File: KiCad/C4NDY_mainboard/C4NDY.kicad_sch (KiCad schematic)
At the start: 45 parts, among them J1 Conn_01x08, J2 Conn_01x07, J3 Conn_01x05, J4 5077CR-16SMC2-BK-TR, J5 Conn_01x06, J6 Conn_01x08, J7 FTSH-105-01-L-DV-K, SW1 SKRPABE010, SW2 SKRPABE010, U1 MIC39100-3.3WS, U2 IS66WVS2M8BLL, U3 STM32G4A1CETx, X1 SG-310SCF

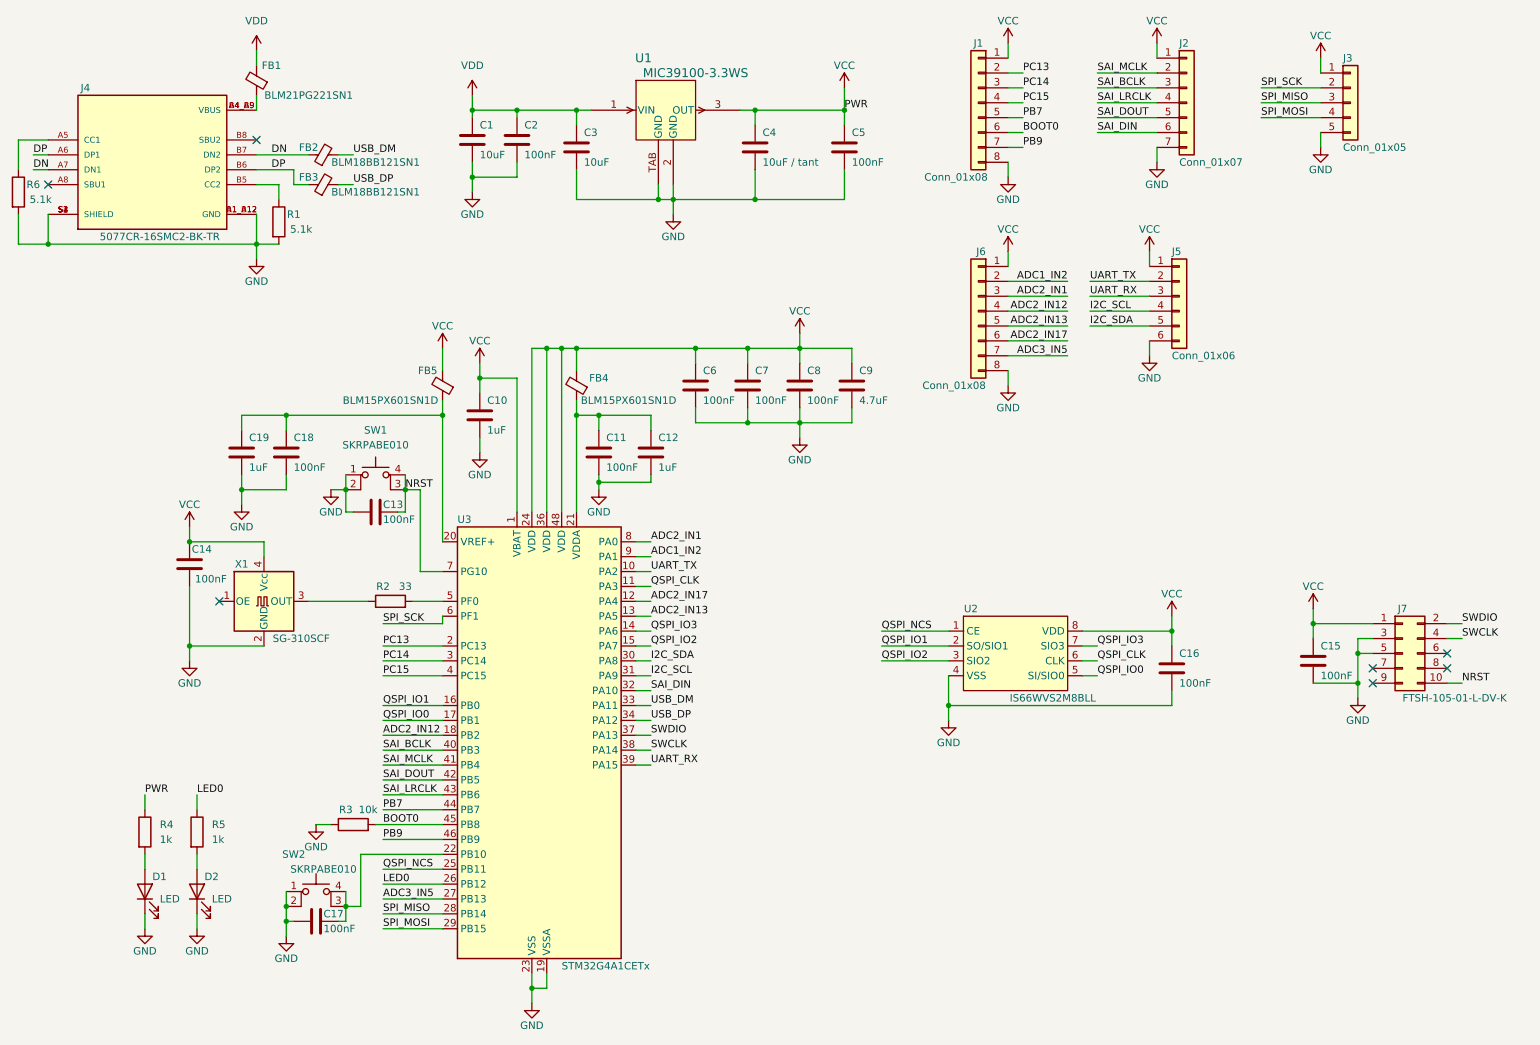
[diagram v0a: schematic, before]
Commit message: SWD用のコネクタを汎用のピンヘッダに変更し、viaをテントに修正。
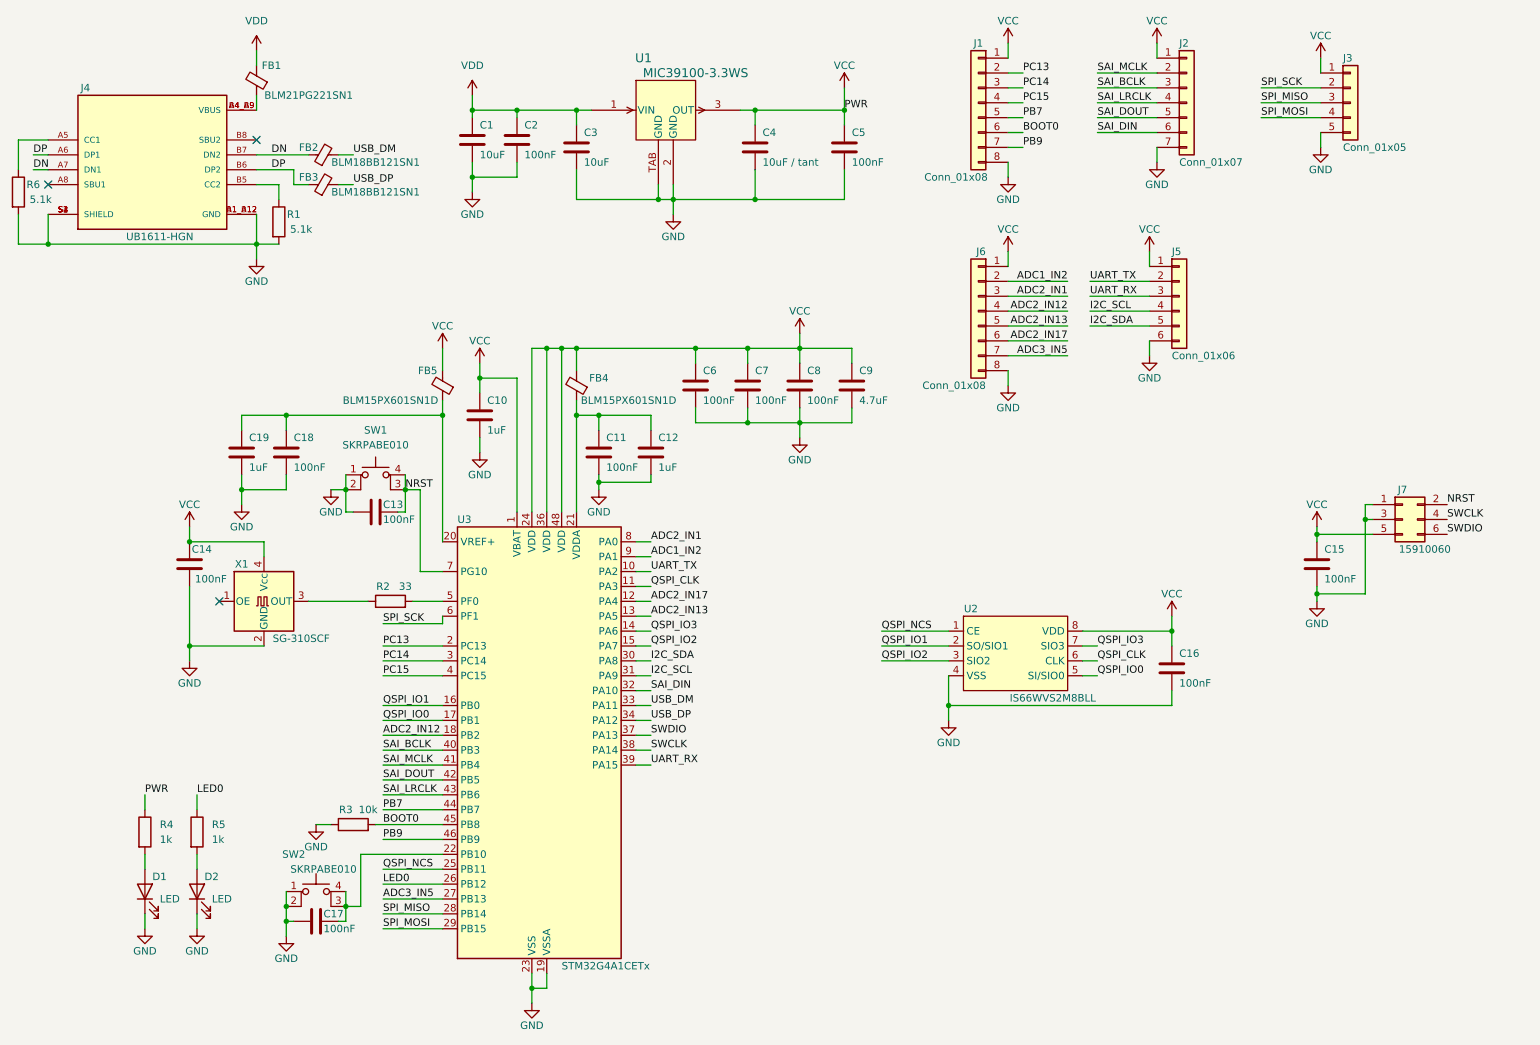
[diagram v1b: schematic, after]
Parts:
- removed J7: FTSH-105-01-L-DV-K, My_Parts:SAMTEC_FTSH-105-XX-X-DV, symbol Connector_Generic:Conn_02x05_Odd_Even
- added J7: 15910060, My_Parts:Molex_15910060, symbol Connector_Generic:Conn_02x03_Odd_Even
- J4: value 5077CR-16SMC2-BK-TR -> UB1611-HGN; footprint My_Parts:NELTRON_5077CR-16SMC2-BK-TR -> My_Parts:Gangyuan_UB1611-HGN; MANUFACTURER Neltron -> Gangyuan; SNAPEDA_PN 5077CR-16SMC2-BK-TR -> UB1611-HGN
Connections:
- net GND: now also J7.1 (Pin_1), J7.3 (Pin_3)
- net NRST: now also J7.2 (Pin_2)
- net SWCLK: now also J7.4 (Pin_4)
- net SWDIO: now also J7.6 (Pin_6)
- net VCC: now also J7.5 (Pin_5)
- no-connect marks 7 -> 3
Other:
- moved on the sheet: C15

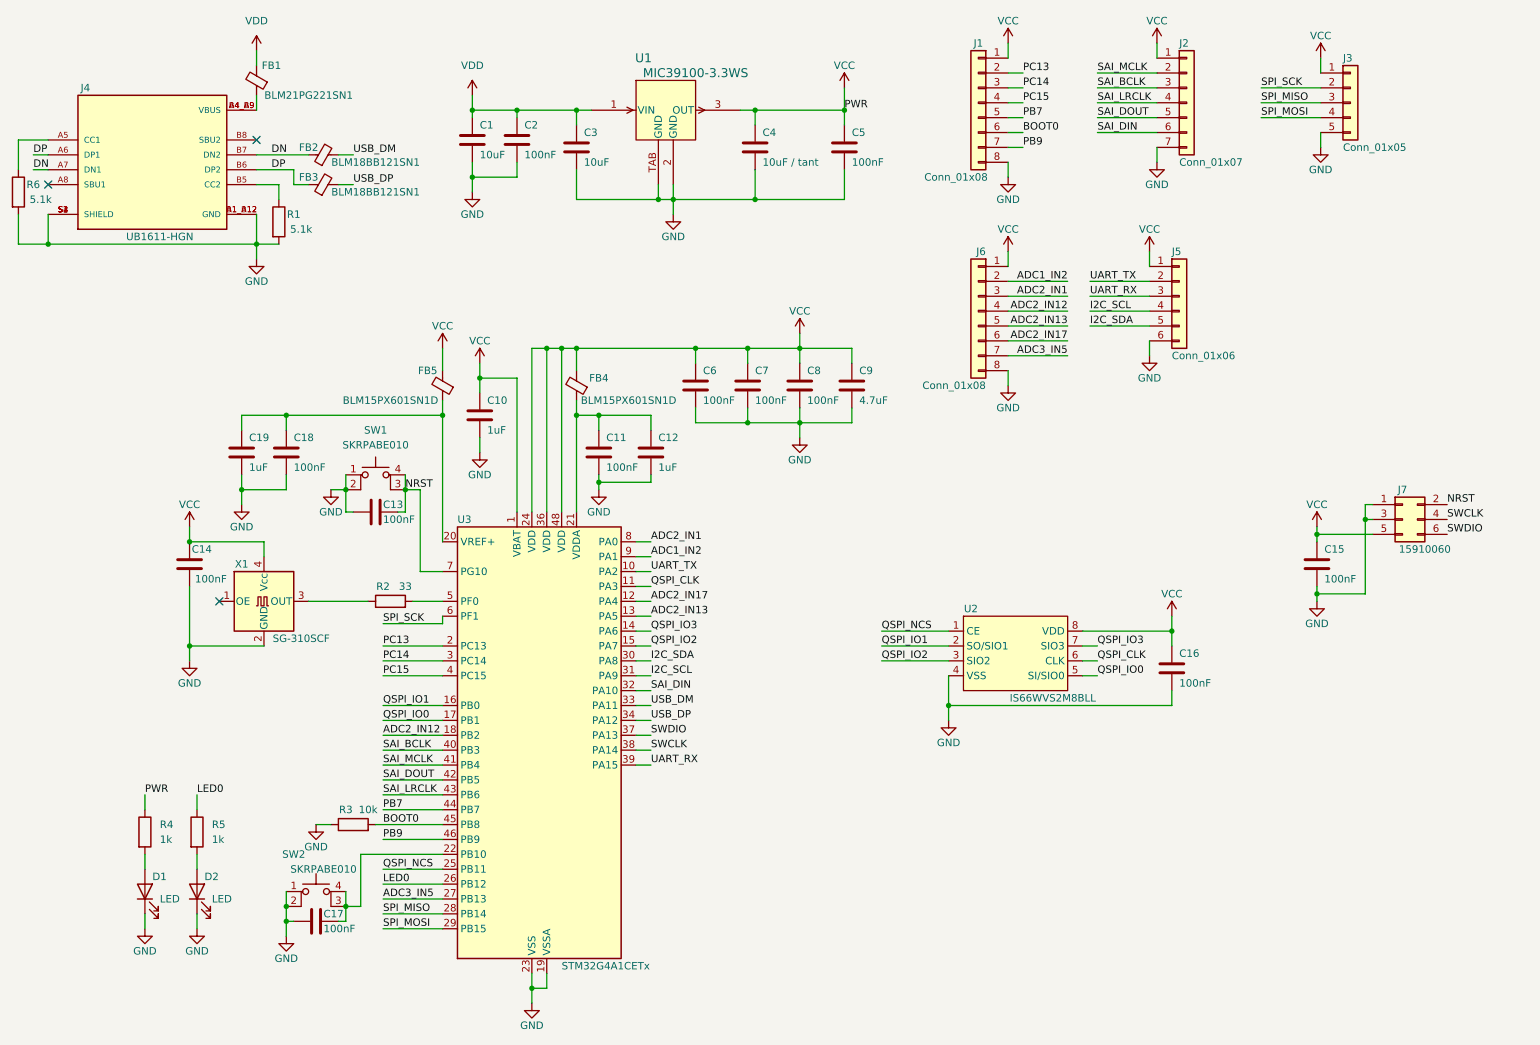
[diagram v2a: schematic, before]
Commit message: Added TPS2116 and removed onboard QSPI..
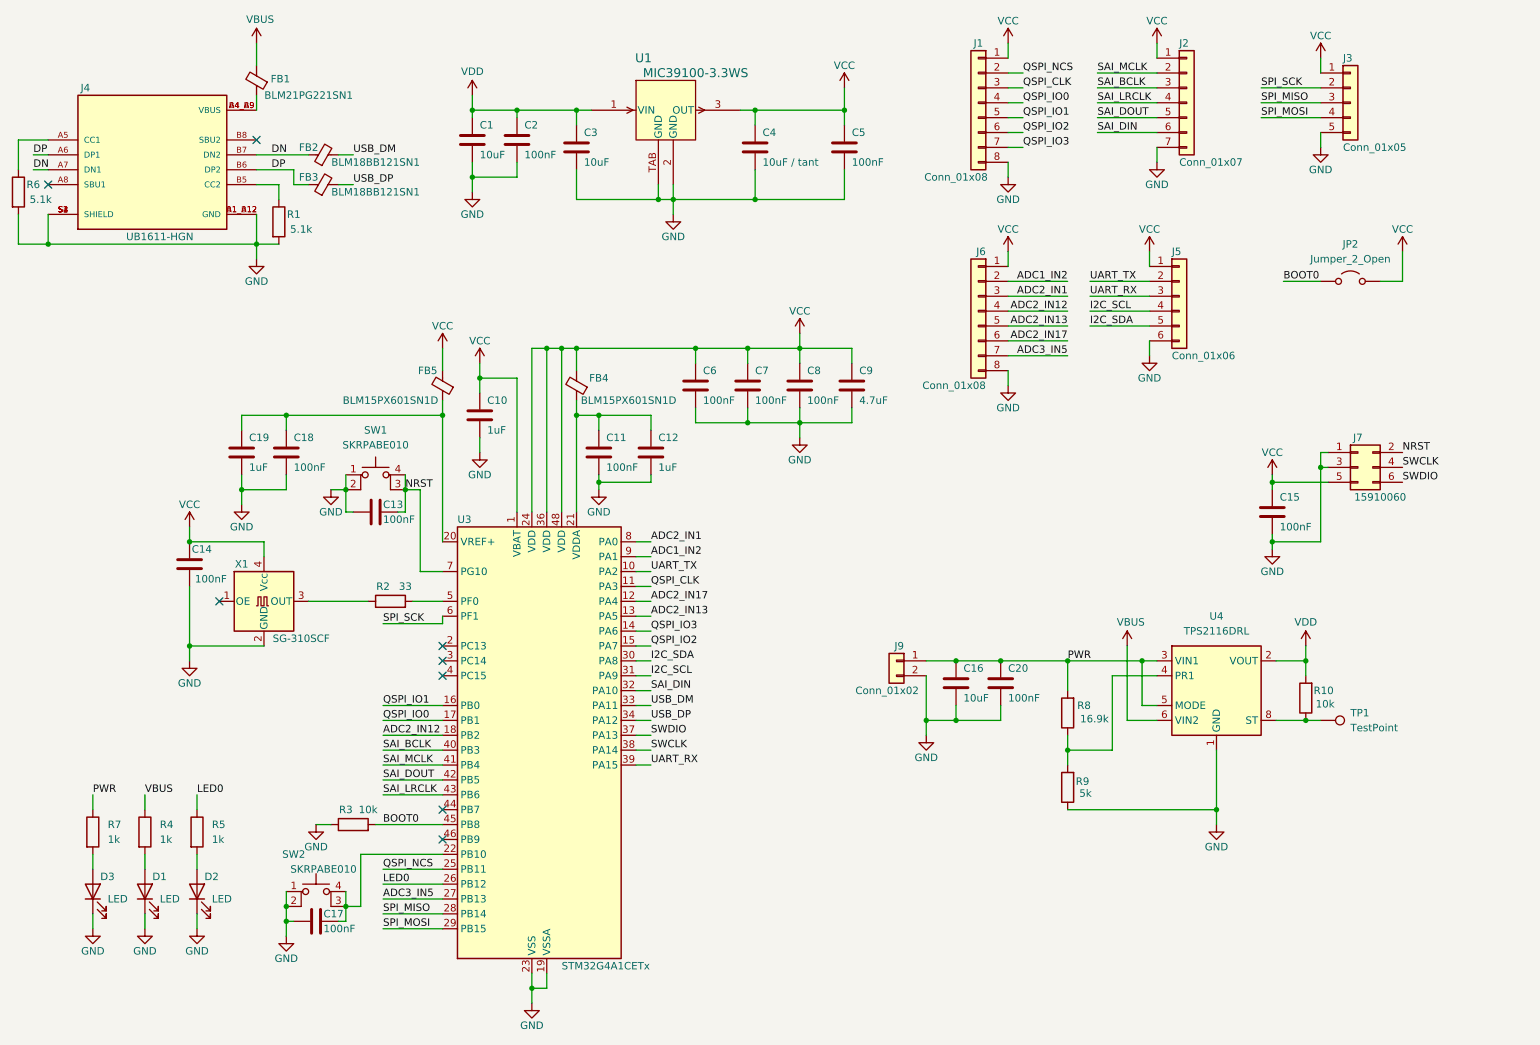
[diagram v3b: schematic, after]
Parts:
- removed U2: IS66WVS2M8BLL, Package_SO:SOIC-8_3.9x4.9mm_P1.27mm, symbol My_Parts:SRAM_QSPI
- added C20: 100nF, Capacitor_SMD:C_0603_1608Metric, symbol Device:C
- added D3: LED, LED_SMD:LED_0603_1608Metric, symbol Device:LED
- added J9: Conn_01x02, My_Parts:PinHeader_1x02_P2.54mm_Vertical, symbol Connector_Generic:Conn_01x02
- added JP2: Jumper_2_Open, Jumper:SolderJumper-2_P1.3mm_Open_RoundedPad1.0x1.5mm, symbol Jumper:Jumper_2_Open
- added R10: 10k, Resistor_SMD:R_0402_1005Metric, symbol Device:R
- added R7: 1k, Resistor_SMD:R_0402_1005Metric, symbol Device:R
- added R8: 16.9k, Resistor_SMD:R_0402_1005Metric, symbol Device:R
- added R9: 5k, Resistor_SMD:R_0402_1005Metric, symbol Device:R
- added TP1: TestPoint, TestPoint:TestPoint_THTPad_1.0x1.0mm_Drill0.5mm, symbol Connector:TestPoint
- added U4: TPS2116DRL, My_Parts:SOT-583-8, symbol Power_Management:TPS2116DRL
- C16: value 100nF -> 10uF; footprint Capacitor_SMD:C_0402_1005Metric -> Capacitor_SMD:C_0603_1608Metric
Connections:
- net BOOT0: now also JP2.1 (A); no longer J1.6 (Pin_6)
- net GND: now also C20.2, D3.1 (K), J9.2 (Pin_2), R9.1, U4.1 (GND)
- net QSPI_CLK: now also J1.3 (Pin_3)
- net QSPI_IO0: now also J1.4 (Pin_4)
- net QSPI_IO1: now also J1.5 (Pin_5)
- net QSPI_IO2: now also J1.6 (Pin_6)
- net QSPI_IO3: now also J1.7 (Pin_7)
- net QSPI_NCS: now also J1.2 (Pin_2)
- net VCC: now also JP2.2 (B); no longer C16.1, R4.1
- net VDD: now also R10.2, U4.2 (VOUT), U4.7 (VOUT); no longer FB1.2
- net PB7: no longer names the net of U3.44 (PB7)
- net PB7: no longer J1.5 (Pin_5)
- net PB9: no longer names the net of U3.46 (PB9)
- net PB9: no longer J1.7 (Pin_7)
- net PC13: no longer names the net of U3.2 (PC13)
- net PC13: no longer J1.2 (Pin_2)
- net PC14: no longer names the net of U3.3 (PC14)
- net PC14: no longer J1.3 (Pin_3)
- net PC15: no longer names the net of U3.4 (PC15)
- net PC15: no longer J1.4 (Pin_4)
- new net: R10.1, TP1.1, U4.8 (ST)
- new net: D3.2 (A), R7.2
- new net: R8.1, R9.2, U4.4 (PR1)
- new net PWR: C16.1, C20.1, J9.1 (Pin_1), R7.1, R8.2, U4.3 (VIN1), U4.5 (MODE)
- new net VBUS: FB1.2, R4.1, U4.6 (VIN2)
- no-connect marks 3 -> 8
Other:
- moved on the sheet: C15, J7
